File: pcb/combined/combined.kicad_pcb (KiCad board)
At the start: 2 copper layers, 124.8 x 87.6 mm, 80 parts, among them J1 5V SCREEN, J10 PRESSURE, J11 XIAO D0-D6, J12 XIAO D7-5V, J2 MAINS_IN, J3 VALVE, J5 CAN BUS, J6 FLOW HALL, J7 24V IN, J8 BOILER SSR, J9 PUMP, Q1 SS8050, Q2 BT136S, Q5 AO3401A, Q6 2N7002, U1 MOC3043M, U10 LMR33630ADDAR, U4 TJA1051T/3, U5 TMP102AIDRLR, U6 ADS1115IDGST, U8 EL817C, U9 EL817C

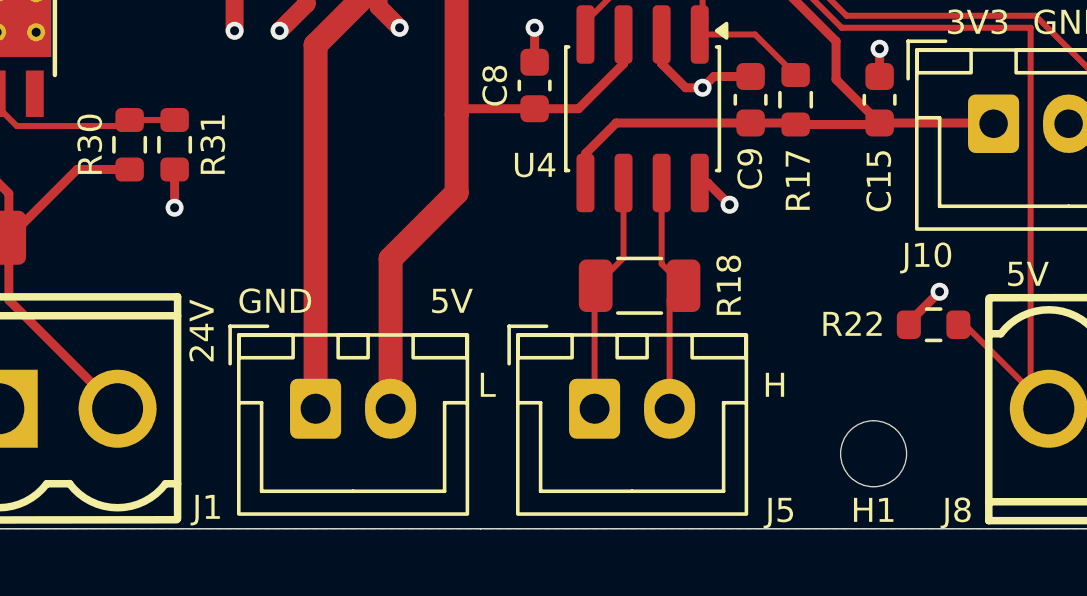
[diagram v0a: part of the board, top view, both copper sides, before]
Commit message: Merge the combined screen 5 V and CAN connectors into one XH 4
J1 (5 V) and J5 (CAN) fed the same cable to the screen. One B4B-XH-A,
the part of J9, now carries 1 GND, 2 +5V, 3 CAN_L, 4 CAN_H and drops
C158012 from the extended parts. J1 takes the J9 placement corrections.

Co-Authored-By: Claude Opus 5.5 <noreply@anthropic.com>
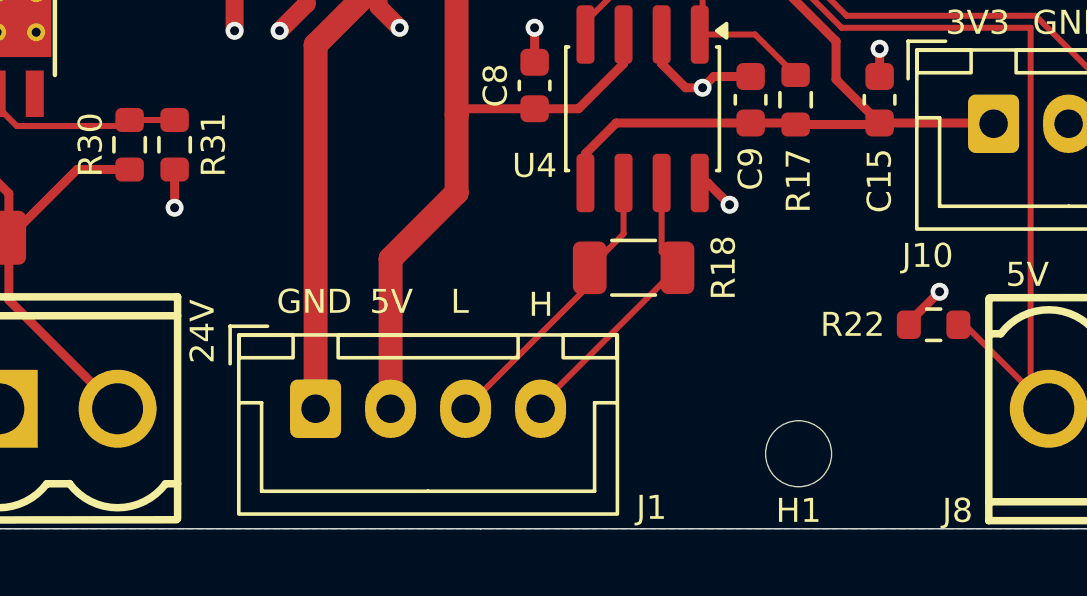
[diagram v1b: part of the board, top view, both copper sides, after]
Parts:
- removed J5: CAN BUS, Connector_JST:JST_XH_B2B-XH-A_1x02_P2.50mm_Vertical
- J1: value 5V SCREEN -> SCREEN; footprint Connector_JST:JST_XH_B2B-XH-A_1x02_P2.50mm_Vertical -> Connector_JST:JST_XH_B4B-XH-A_1x04_P2.50mm_Vertical
- moved H1 2.50 mm to (91.0, 132.1)
- moved R18 0.63 mm to (85.5, 125.9)
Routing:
- net /Interfaces/CAN_L: track 7.92 -> 9.71 mm
- net /Interfaces/CAN_H: track 8.02 -> 9.63 mm

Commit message: Lower the combined XIAO sockets to the 5 mm Hong Cheng header
J11/J12 move from the 8.5 mm hanxia socket (C22438157) to the Hong Cheng
HC-PM254-5.0H-1x7PZ (C27985232), the height Seeed uses on its XIAO boards.
The footprint takes the maker's 1.02 mm holes, its 18.18 x 2.4 mm body and
the LCSC 3D model. The supplier footprint matches the former one, so the
J11/J12 placement correction stays; the JLCPCB preview confirmed it.

Co-Authored-By: Claude Opus 5.5 <noreply@anthropic.com>
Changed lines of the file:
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@@
 			)
 		)
-		(property "MPN" "HX PM2.54-1x7P ZC-Y"
+		(property "MPN" "HC-PM254-5.0H-1x7PZ"
 			(at 0 0 180)
 			(unlocked yes)
@@
 			)
 		)
-		(property "LCSC" "C22438157"
+		(property "LCSC" "C27985232"
 			(at 0 0 180)
 			(unlocked yes)
@@
 		(duplicate_pad_numbers_are_jumpers no)
 		(fp_rect
-			(start -1.525 -1.525)
-			(end 1.525 16.765)
+			(start -1.45 -1.72)
+			(end 1.45 16.96)
 			(stroke
 				(width 0.05)
@@
 		)
 		(fp_line
-			(start 1.27 16.51)
-			(end -1.27 16.51)
+			(start 1.2 16.71)
+			(end -1.2 16.71)
 			(stroke
 				(width 0.1)
@@
 		)
 		(fp_line
-			(start 1.27 -0.635)
-			(end 1.27 16.51)
+			(start 1.2 -0.87)
+			(end 1.2 16.71)
 			(stroke
 				(width 0.1)
@@
 		)
 		(fp_line
-			(start 0.635 -1.27)
-			(end 1.27 -0.635)
+			(start 0.6 -1.47)
+			(end 1.2 -0.87)
 			(stroke
 				(width 0.1)
@@
 		)
 		(fp_line
-			(start -1.27 16.51)
-			(end -1.27 -1.27)
+			(start -1.2 16.71)
+			(end -1.2 -1.47)
 			(stroke
 				(width 0.1)
@@
 		)
 		(fp_line
-			(start -1.27 -1.27)
-			(end 0.635 -1.27)
+			(start -1.2 -1.47)
+			(end 0.6 -1.47)
 			(stroke
 				(width 0.1)
@@
 			(at 0 0 180)
 			(size 1.7 1.7)
-			(drill 1)
+			(drill 1.02)
 			(layers "*.Cu" "*.Mask")
 			(remove_unused_layers no)
@@
 			(at 0 2.54 180)
 			(size 1.7 1.7)
-			(drill 1)
+			(drill 1.02)
 			(layers "*.Cu" "*.Mask")
 			(remove_unused_layers no)
@@
 			(at 0 5.08 180)
 			(size 1.7 1.7)
-			(drill 1)
+			(drill 1.02)
 			(layers "*.Cu" "*.Mask")
 			(remove_unused_layers no)
@@
 			(at 0 7.62 180)
 			(size 1.7 1.7)
-			(drill 1)
+			(drill 1.02)
 			(layers "*.Cu" "*.Mask")
 			(remove_unused_layers no)
@@
 			(at 0 10.16 180)
 			(size 1.7 1.7)
-			(drill 1)
+			(drill 1.02)
 			(layers "*.Cu" "*.Mask")
 			(remove_unused_layers no)
@@
 			(at 0 12.7 180)
 			(size 1.7 1.7)
-			(drill 1)
+			(drill 1.02)
 			(layers "*.Cu" "*.Mask")
 			(remove_unused_layers no)
@@
 			(at 0 15.24 180)
 			(size 1.7 1.7)
-			(drill 1)
+			(drill 1.02)
 			(layers "*.Cu" "*.Mask")
 			(remove_unused_layers no)
@@
 		)
 		(embedded_fonts no)
-		(model "${KICAD10_3DMODEL_DIR}/Connector_PinSocket_2.54mm.3dshapes/PinSocket_1x07_P2.54mm_Vertical.step"
+		(model "${KIPRJMOD}/Combined_Local.3dshapes/HC-PM254-5.0H-1x7PZ.wrl"
 			(offset
-				(xyz 0 0 0)
+				(xyz 0 -7.62 0)
 			)
 			(scale
@@
 			)
 			(rotate
-				(xyz 0 0 0)
+				(xyz 0 0 90)
 			)
 		)
@@
 			)
 		)
-		(property "MPN" "HX PM2.54-1x7P ZC-Y"
+		(property "MPN" "HC-PM254-5.0H-1x7PZ"
 			(at 0 0 0)
 			(unlocked yes)
@@
 			)
 		)
-		(property "LCSC" "C22438157"
+		(property "LCSC" "C27985232"
 			(at 0 0 0)
 			(unlocked yes)
@@
 		(duplicate_pad_numbers_are_jumpers no)
 		(fp_rect
-			(start -1.525 -1.525)
-			(end 1.525 16.765)
+			(start -1.45 -1.72)
+			(end 1.45 16.96)
 			(stroke
 				(width 0.05)
@@
 		)
 		(fp_line
-			(start -1.27 -1.27)
-			(end 0.635 -1.27)
+			(start -1.2 -1.47)
+			(end 0.6 -1.47)
 			(stroke
 				(width 0.1)
@@
 		)
 		(fp_line
-			(start -1.27 16.51)
-			(end -1.27 -1.27)
+			(start -1.2 16.71)
+			(end -1.2 -1.47)
 			(stroke
 				(width 0.1)
@@
 		)
 		(fp_line
-			(start 0.635 -1.27)
-			(end 1.27 -0.635)
+			(start 0.6 -1.47)
+			(end 1.2 -0.87)
 			(stroke
 				(width 0.1)
@@
 		)
 		(fp_line
-			(start 1.27 -0.635)
-			(end 1.27 16.51)
+			(start 1.2 -0.87)
+			(end 1.2 16.71)
 			(stroke
 				(width 0.1)
@@
 		)
 		(fp_line
-			(start 1.27 16.51)
-			(end -1.27 16.51)
+			(start 1.2 16.71)
+			(end -1.2 16.71)
 			(stroke
 				(width 0.1)
@@
 			(at 0 0)
 			(size 1.7 1.7)
-			(drill 1)
+			(drill 1.02)
 			(layers "*.Cu" "*.Mask")
 			(remove_unused_layers no)
@@
 			(at 0 2.54)
 			(size 1.7 1.7)
-			(drill 1)
+			(drill 1.02)
 			(layers "*.Cu" "*.Mask")
 			(remove_unused_layers no)
@@
 			(at 0 5.08)
 			(size 1.7 1.7)
-			(drill 1)
+			(drill 1.02)
 			(layers "*.Cu" "*.Mask")
 			(remove_unused_layers no)
@@
 			(at 0 7.62)
 			(size 1.7 1.7)
-			(drill 1)
+			(drill 1.02)
 			(layers "*.Cu" "*.Mask")
 			(remove_unused_layers no)
@@
 			(at 0 10.16)
 			(size 1.7 1.7)
-			(drill 1)
+			(drill 1.02)
 			(layers "*.Cu" "*.Mask")
 			(remove_unused_layers no)
@@
 			(at 0 12.7)
 			(size 1.7 1.7)
-			(drill 1)
+			(drill 1.02)
 			(layers "*.Cu" "*.Mask")
 			(remove_unused_layers no)
@@
 			(at 0 15.24)
 			(size 1.7 1.7)
-			(drill 1)
+			(drill 1.02)
 			(layers "*.Cu" "*.Mask")
 			(remove_unused_layers no)
@@
 		)
 		(embedded_fonts no)
-		(model "${KICAD10_3DMODEL_DIR}/Connector_PinSocket_2.54mm.3dshapes/PinSocket_1x07_P2.54mm_Vertical.step"
+		(model "${KIPRJMOD}/Combined_Local.3dshapes/HC-PM254-5.0H-1x7PZ.wrl"
 			(offset
-				(xyz 0 0 0)
+				(xyz 0 -7.62 0)
 			)
 			(scale
@@
 			)
 			(rotate
-				(xyz 0 0 0)
+				(xyz 0 0 90)
 			)
 		)

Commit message: Model the combined board for enclosure design; J2/J3 flush with the edge
print/parts/combined becomes a stand-in for the board instead of the
footprint plate: exact outline, 1.6 mm thick, the six M2 holes, and the
tall components as four-walled boxes (XH, HT396V and HT396R connectors,
and the XIAO at 15 mm above the PCB underside). Sizes come from the 3D
models placed as on the board and match the Kefa and JST drawings added
in docs/jlcpcb.

On the board, J2 and J3 move 0.2 mm east so their front face is flush with
the east edge, with the traces adjusted around them and around J1.

Co-Authored-By: Claude Opus 5.5 <noreply@anthropic.com>
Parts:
- moved J2 0.20 mm to (171.1, 76.6)
- moved J3 0.20 mm to (171.1, 64.3)
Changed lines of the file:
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@@
 	(footprint "Combined_Local:CONN-TH_P3.96_HT396R-3.96-2P"
 		(layer "F.Cu")
-		(at 170.9 76.6 90)
+		(at 171.1 76.6 90)
 		(property "Reference" "J2"
 			(at 4.8 4.1 0)
@@
 	(footprint "Combined_Local:CONN-TH_P3.96_HT396R-3.96-2P"
 		(layer "F.Cu")
-		(at 170.9 64.26 90)
+		(at 171.1 64.26 90)
 		(property "Reference" "J3"
 			(at -4.84 4 0)
@@
 	)
 	(segment
-		(start 84.0375 125.9)
-		(end 84.0375 126.4625)
-		(width 0.2)
-		(layer "F.Cu")
-		(net "/Interfaces/CAN_L")
-	)
-	(segment
-		(start 85.165 124.7725)
-		(end 84.0375 125.9)
-		(width 0.2)
-		(layer "F.Cu")
-		(net "/Interfaces/CAN_L")
-	)
-	(segment
-		(start 85.165 123.075)
-		(end 85.165 124.7725)
-		(width 0.2)
-		(layer "F.Cu")
-		(net "/Interfaces/CAN_L")
-	)
-	(segment
-		(start 84.0375 126.4625)
-		(end 79.9 130.6)
-		(width 0.2)
-		(layer "F.Cu")
-		(net "/Interfaces/CAN_L")
-	)
-	(segment
-		(start 86.435 123.075)
-		(end 86.435 125.3725)
-		(width 0.2)
-		(layer "F.Cu")
-		(net "/Interfaces/CAN_H")
-	)
-	(segment
-		(start 86.435 125.3725)
-		(end 86.9625 125.9)
-		(width 0.2)
-		(layer "F.Cu")
-		(net "/Interfaces/CAN_H")
-	)
-	(segment
-		(start 82.4 130.4625)
-		(end 82.4 130.6)
-		(width 0.2)
-		(layer "F.Cu")
-		(net "/Interfaces/CAN_H")
-	)
-	(segment
-		(start 86.9625 125.9)
-		(end 82.4 130.4625)
-		(width 0.2)
-		(layer "F.Cu")
-		(net "/Interfaces/CAN_H")
-	)
-	(segment
 		(start 96.1 60.2325)
 		(end 96.1 61.985)
@@
 	)
 	(segment
+		(start 157 78.5)
+		(end 171.02 78.5)
+		(width 1)
+		(layer "F.Cu")
+		(net "/L_IN")
+	)
+	(segment
 		(start 157.08 78.58)
 		(end 157 78.5)
@@
 	)
 	(segment
-		(start 170.9 78.58)
-		(end 157.08 78.58)
+		(start 171.02 78.5)
+		(end 171.1 78.58)
 		(width 1)
 		(layer "F.Cu")
@@
 	)
 	(segment
-		(start 170.9 66.24)
-		(end 170.9 74.62)
+		(start 171.1 66.24)
+		(end 171.1 74.62)
 		(width 1)
 		(layer "F.Cu")
@@
 	)
 	(segment
+		(start 84.0375 125.9)
+		(end 84.0375 126.4625)
+		(width 0.2)
+		(layer "F.Cu")
+		(net "/Interfaces/CAN_L")
+	)
+	(segment
+		(start 85.165 124.7725)
+		(end 84.0375 125.9)
+		(width 0.2)
+		(layer "F.Cu")
+		(net "/Interfaces/CAN_L")
+	)
+	(segment
+		(start 85.165 123.075)
+		(end 85.165 124.7725)
+		(width 0.2)
+		(layer "F.Cu")
+		(net "/Interfaces/CAN_L")
+	)
+	(segment
+		(start 84.0375 126.4625)
+		(end 79.9 130.6)
+		(width 0.2)
+		(layer "F.Cu")
+		(net "/Interfaces/CAN_L")
+	)
+	(segment
+		(start 86.435 123.075)
+		(end 86.435 125.3725)
+		(width 0.2)
+		(layer "F.Cu")
+		(net "/Interfaces/CAN_H")
+	)
+	(segment
+		(start 86.435 125.3725)
+		(end 86.9625 125.9)
+		(width 0.2)
+		(layer "F.Cu")
+		(net "/Interfaces/CAN_H")
+	)
+	(segment
+		(start 82.4 130.4625)
+		(end 82.4 130.6)
+		(width 0.2)
+		(layer "F.Cu")
+		(net "/Interfaces/CAN_H")
+	)
+	(segment
+		(start 86.9625 125.9)
+		(end 82.4 130.4625)
+		(width 0.2)
+		(layer "F.Cu")
+		(net "/Interfaces/CAN_H")
+	)
+	(segment
 		(start 97.6 60.2325)
 		(end 101.1475 60.2325)
@@
 	)
 	(segment
-		(start 170.9 62.28)
-		(end 124.135 62.28)
+		(start 124.135 62.28)
+		(end 171.1 62.28)
 		(width 1)
 		(layer "B.Cu")

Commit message: Turn J7 so its plug latch faces south, like J8
The HT396K plug is 2.6 mm deeper than its header on the latch side. With
J7 turned 180 degrees, both 24 V and boiler plugs latch out through the
south wall of the enclosure. Its pins are swapped in the schematic so GND
stays on the left, next to U10. Adds the Kefa HT396K plug drawings.

Co-Authored-By: Claude Opus 5.5 <noreply@anthropic.com>
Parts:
- turned J7 to 180 degrees
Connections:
- J7 pad 1: GND -> +24V
- J7 pad 2: +24V -> GND
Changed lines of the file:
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@@
 	(footprint "Combined_Local:CONN-TH_P3.96_HT396V-3.96-2P"
 		(layer "F.Cu")
-		(at 66.32 130.6)
+		(at 66.32 130.6 180)
 		(property "Reference" "J7"
-			(at -4.92 3.3 0)
+			(at 5.02 -3.3 180)
 			(layer "F.SilkS")
 			(effects
@@
 		)
 		(property "Value" "24V IN"
-			(at 0.005 -2.3 0)
+			(at 0.005 -2.3 180)
 			(layer "F.Fab")
 			(effects
@@
 		)
 		(property "Datasheet" ""
-			(at 0 0 0)
+			(at 0 0 180)
 			(layer "F.Fab")
 			(hide yes)
@@
 		)
 		(property "Description" ""
-			(at 0 0 0)
+			(at 0 0 180)
 			(layer "F.Fab")
 			(hide yes)
@@
 		)
 		(property "MPN" "HT396V-3.96-2P"
-			(at 0 0 270)
+			(at 0 0 90)
 			(layer "F.SilkS")
 			(hide yes)
@@
 		)
 		(property "LCSC" "C577788"
-			(at 0 0 270)
+			(at 0 0 90)
 			(layer "F.SilkS")
 			(hide yes)
@@
 		)
 		(property "Note" "Kefa HT396V vertical header; mating plug HT396K-3.96-2P (C577777, screw), 1 GND, 2 +24V, from the Wago split of the 24 V supply"
-			(at 0 0 270)
+			(at 0 0 90)
 			(layer "F.SilkS")
 			(hide yes)
@@
 		(duplicate_pad_numbers_are_jumpers no)
 		(fp_line
+			(start 3.98 -3.73)
+			(end 3.98 3.67)
+			(stroke
+				(width 0.25)
+				(type solid)
+			)
+			(layer "F.SilkS")
+		)
+		(fp_line
+			(start 3.58 2.5)
+			(end 3.98 2.5)
+			(stroke
+				(width 0.25)
+				(type solid)
+			)
+			(layer "F.SilkS")
+		)
+		(fp_line
+			(start -0.38 2.5)
+			(end 0.38 2.5)
+			(stroke
+				(width 0.25)
+				(type solid)
+			)
+			(layer "F.SilkS")
+		)
+		(fp_line
+			(start -3.58 2.5)
+			(end -3.97 2.5)
+			(stroke
+				(width 0.25)
+				(type solid)
+			)
+			(layer "F.SilkS")
+		)
+		(fp_line
+			(start -3.97 3.71)
+			(end 3.95 3.7)
+			(stroke
+				(width 0.25)
+				(type solid)
+			)
+			(layer "F.SilkS")
+		)
+		(fp_line
+			(start -3.97 -3.1)
+			(end 3.98 -3.1)
+			(stroke
+				(width 0.25)
+				(type solid)
+			)
+			(layer "F.SilkS")
+		)
+		(fp_line
+			(start -3.97 -3.71)
+			(end -3.97 3.69)
+			(stroke
+				(width 0.25)
+				(type solid)
+			)
+			(layer "F.SilkS")
+		)
+		(fp_line
 			(start -3.97 -3.73)
 			(end 3.98 -3.73)
@@
 			(layer "F.SilkS")
 		)
-		(fp_line
-			(start -3.97 -3.71)
-			(end -3.97 3.69)
-			(stroke
-				(width 0.25)
-				(type solid)
-			)
-			(layer "F.SilkS")
-		)
-		(fp_line
-			(start -3.97 -3.1)
-			(end 3.98 -3.1)
-			(stroke
-				(width 0.25)
-				(type solid)
-			)
-			(layer "F.SilkS")
-		)
-		(fp_line
-			(start -3.97 3.71)
-			(end 3.95 3.7)
-			(stroke
-				(width 0.25)
-				(type solid)
-			)
-			(layer "F.SilkS")
-		)
-		(fp_line
-			(start -3.58 2.5)
-			(end -3.97 2.5)
-			(stroke
-				(width 0.25)
-				(type solid)
-			)
-			(layer "F.SilkS")
-		)
-		(fp_line
+		(fp_arc
+			(start 3.58 2.5)
+			(mid 1.976164 3.299996)
+			(end 0.375408 2.493853)
+			(stroke
+				(width 0.25)
+				(type solid)
+			)
+			(layer "F.SilkS")
+		)
+		(fp_arc
 			(start -0.38 2.5)
-			(end 0.38 2.5)
-			(stroke
-				(width 0.25)
-				(type solid)
-			)
-			(layer "F.SilkS")
-		)
-		(fp_line
-			(start 3.58 2.5)
-			(end 3.98 2.5)
-			(stroke
-				(width 0.25)
-				(type solid)
-			)
-			(layer "F.SilkS")
-		)
-		(fp_line
-			(start 3.98 -3.73)
-			(end 3.98 3.67)
+			(mid -0.38 2.5)
+			(end -0.38 2.5)
 			(stroke
 				(width 0.25)
@@
 			(layer "F.SilkS")
 		)
-		(fp_arc
-			(start -0.38 2.5)
-			(mid -0.38 2.5)
-			(end -0.38 2.5)
-			(stroke
-				(width 0.25)
-				(type solid)
-			)
-			(layer "F.SilkS")
-		)
-		(fp_arc
-			(start 3.58 2.5)
-			(mid 1.976164 3.299996)
-			(end 0.375408 2.493853)
-			(stroke
-				(width 0.25)
-				(type solid)
-			)
-			(layer "F.SilkS")
-		)
 		(fp_circle
 			(center -3.96 3.7)
@@
 		)
 		(fp_line
+			(start 4.21 3.95)
+			(end -4.21 3.95)
+			(stroke
+				(width 0.05)
+				(type solid)
+			)
+			(layer "F.CrtYd")
+		)
+		(fp_line
+			(start 4.21 -3.95)
+			(end 4.21 3.95)
+			(stroke
+				(width 0.05)
+				(type solid)
+			)
+			(layer "F.CrtYd")
+		)
+		(fp_line
+			(start -4.21 3.95)
+			(end -4.21 -3.95)
+			(stroke
+				(width 0.05)
+				(type solid)
+			)
+			(layer "F.CrtYd")
+		)
+		(fp_line
 			(start -4.21 -3.95)
 			(end 4.21 -3.95)
@@
 			(layer "F.CrtYd")
 		)
-		(fp_line
-			(start -4.21 3.95)
-			(end -4.21 -3.95)
-			(stroke
-				(width 0.05)
-				(type solid)
-			)
-			(layer "F.CrtYd")
-		)
-		(fp_line
-			(start 4.21 -3.95)
-			(end 4.21 3.95)
-			(stroke
-				(width 0.05)
-				(type solid)
-			)
-			(layer "F.CrtYd")
-		)
-		(fp_line
-			(start 4.21 3.95)
-			(end -4.21 3.95)
-			(stroke
-				(width 0.05)
-				(type solid)
-			)
-			(layer "F.CrtYd")
-		)
 		(fp_text user "${REFERENCE}"
-			(at 0 0 0)
+			(at 0 0 180)
 			(layer "F.Fab")
 			(effects
@@
 		)
 		(pad "1" thru_hole rect
-			(at -1.98 0)
+			(at -1.98 0 180)
+			(size 2.6 2.6)
+			(drill 1.700022)
+			(layers "*.Cu" "*.Mask")
+			(remove_unused_layers no)
+			(net "+24V")
+			(pinfunction "Pin_1_1")
+			(pintype "passive")
+		)
+		(pad "2" thru_hole circle
+			(at 1.98 0 180)
 			(size 2.6 2.6)
 			(drill 1.700022)
@@
 			(remove_unused_layers no)
 			(net "GND")
-			(pinfunction "Pin_1_1")
-			(pintype "passive")
-		)
-		(pad "2" thru_hole circle
-			(at 1.98 0)
-			(size 2.6 2.6)
-			(drill 1.700022)
-			(layers "*.Cu" "*.Mask")
-			(remove_unused_layers no)
-			(net "+24V")
 			(pinfunction "Pin_2_2")
 			(pintype "passive")
